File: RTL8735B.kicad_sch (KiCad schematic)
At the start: 36 parts, among them U1 W25Q128JVSIQ, U2 RTL8735BDM-A20-N04

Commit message: All key features are in the schematic.
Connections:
- net SEN_SYSCLK: now also U2.30 (SSOR_SYSCLK)
- net GPIOD_14 renamed DMIC_CLK
- net GPIOD_18 renamed DMIC_DATA
- net GPIOE_3 renamed BATT_SCL
- net GPIOE_4 renamed BATT_SDA
- net V_USB renamed +5V
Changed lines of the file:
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@@
 	(wire
 		(pts
+			(xy 123.19 135.89) (xy 123.19 163.83)
+		)
+		(stroke
+			(width 0)
+			(type default)
+		)
+	)
+	(wire
+		(pts
 			(xy 57.15 69.85) (xy 68.58 69.85)
 		)
@@
 	(wire
 		(pts
-			(xy 125.73 135.89) (xy 125.73 157.48)
+			(xy 125.73 135.89) (xy 125.73 163.83)
 		)
 		(stroke
@@
 	(wire
 		(pts
-			(xy 123.19 135.89) (xy 123.19 157.48)
-		)
-		(stroke
-			(width 0)
-			(type default)
-		)
-	)
-	(wire
-		(pts
 			(xy 143.51 21.59) (xy 143.51 24.13)
 		)
@@
 		)
 	)
-	(label "GPIOD_14"
+	(label "DMIC_CLK"
 		(at 100.33 158.75 90)
 		(effects
@@
 		)
 	)
-	(label "GPIOD_18"
+	(label "DMIC_DATA"
 		(at 110.49 158.75 90)
 		(effects
@@
 	(global_label "SEN_SYSCLK"
 		(shape input)
-		(at 127 162.56 270)
+		(at 97.79 163.83 270)
 		(fields_autoplaced yes)
 		(effects
@@
 		)
 		(property "Intersheetrefs" "${INTERSHEET_REFS}"
-			(at 127 177.2775 90)
+			(at 97.79 178.5475 90)
 			(effects
 				(font
@@
 		)
 	)
+	(global_label "BATT_SDA"
+		(shape input)
+		(at 125.73 163.83 270)
+		(fields_autoplaced yes)
+		(effects
+			(font
+				(size 1.27 1.27)
+			)
+			(justify right)
+		)
+		(property "Intersheetrefs" "${INTERSHEET_REFS}"
+			(at 125.73 175.6447 90)
+			(effects
+				(font
+					(size 1.27 1.27)
+				)
+				(justify right)
+				(hide yes)
+			)
+		)
+	)
 	(global_label "SEN_SDA"
 		(shape input)
@@
 		)
 	)
+	(global_label "BATT_SCL"
+		(shape input)
+		(at 123.19 163.83 270)
+		(fields_autoplaced yes)
+		(effects
+			(font
+				(size 1.27 1.27)
+			)
+			(justify right)
+		)
+		(property "Intersheetrefs" "${INTERSHEET_REFS}"
+			(at 123.19 175.5842 90)
+			(effects
+				(font
+					(size 1.27 1.27)
+				)
+				(justify right)
+				(hide yes)
+			)
+		)
+	)
 	(symbol
 		(lib_id "Device:R_US")
@@
 			)
 		)
-		(property "Value" "V_USB"
+		(property "Value" "+5V"
 			(at 147.32 13.97 0)
 			(effects

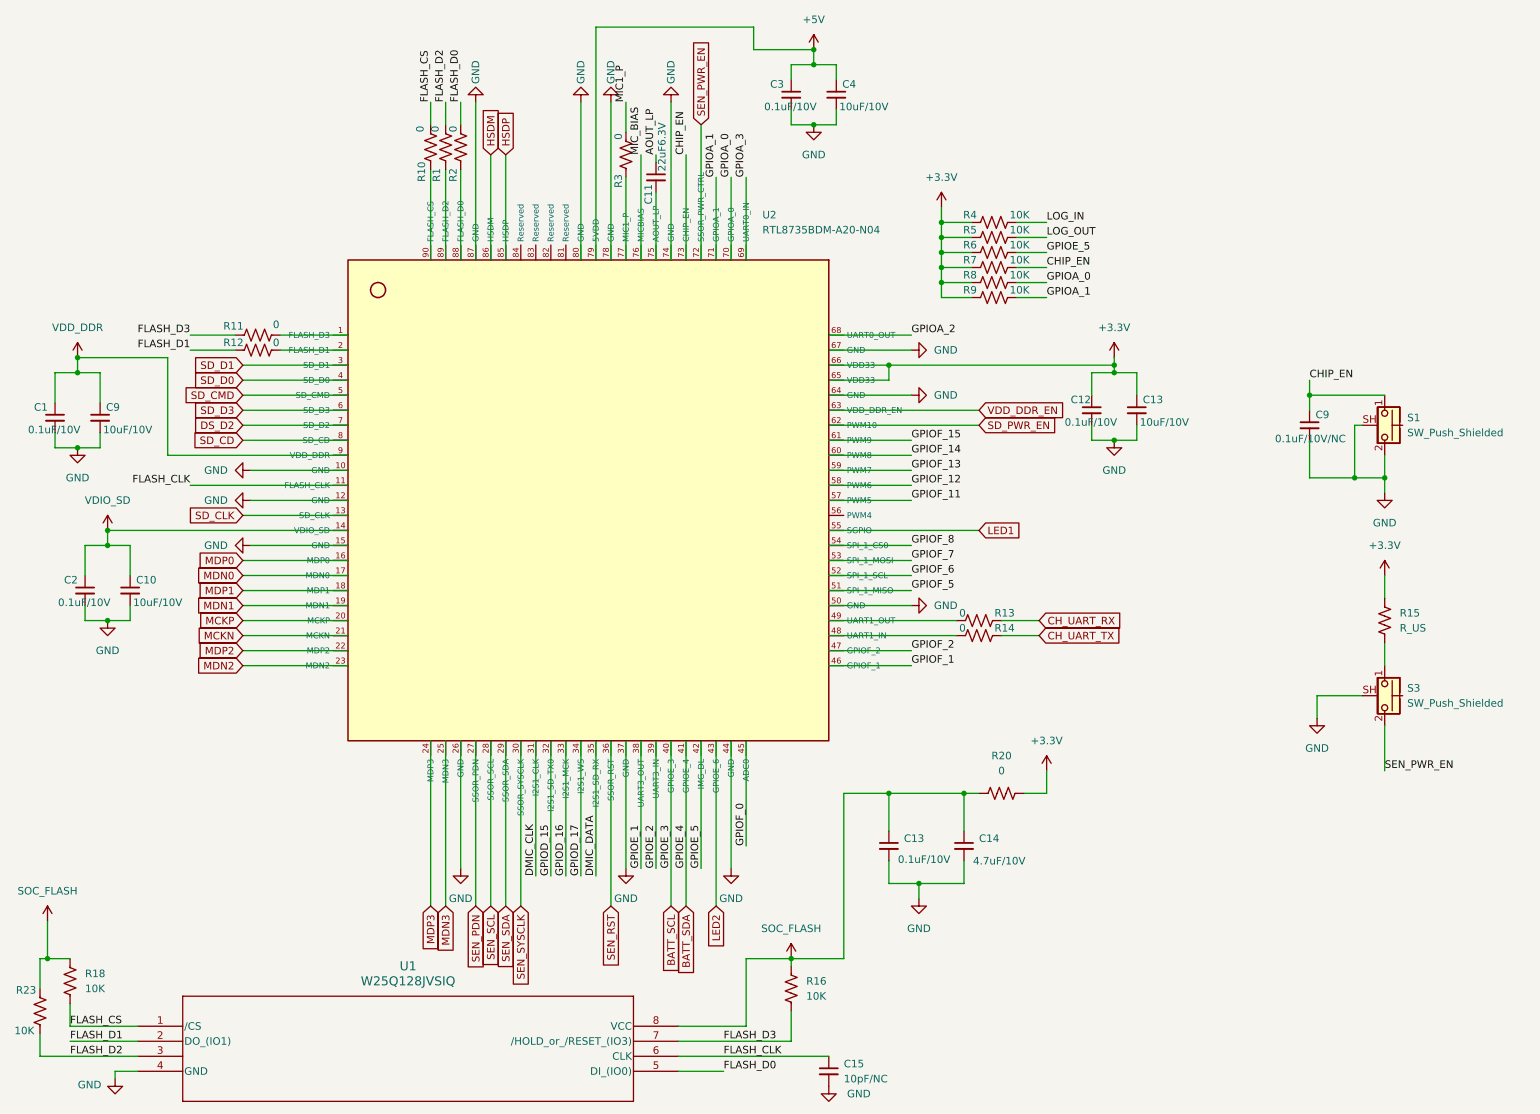
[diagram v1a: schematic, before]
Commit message: All footprints configured correctly. Next step is layout
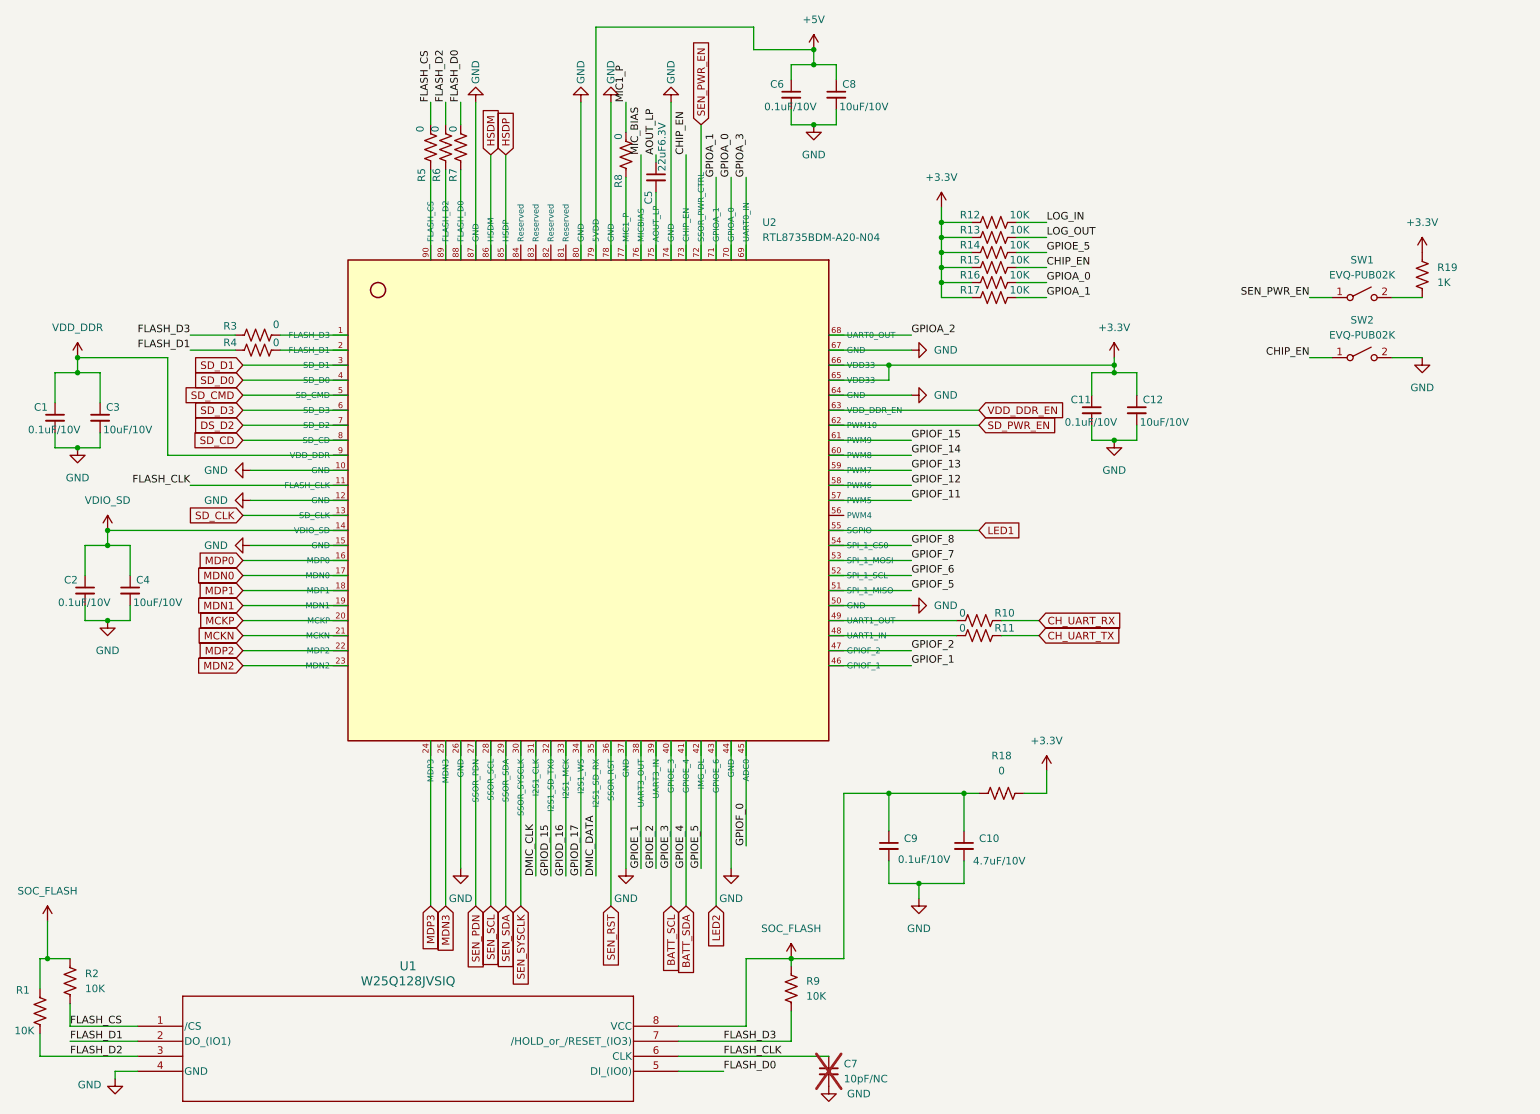
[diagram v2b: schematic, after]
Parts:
- removed C9: 0.1uF/10V/NC, symbol Device:C_Small
- removed R15: R_US, symbol Device:R_US
- removed S1, S3: SW_Push_Shielded, symbol Switch:SW_Push_Shielded
- added R19: 1K, Resistor_SMD:R_0201_0603Metric_Pad0.64x0.40mm_HandSolder, symbol Device:R_US
- added SW1, SW2: EVQ-PUB02K, Button_Switch_SMD:Panasonic_EVQPUK_EVQPUB, symbol Switch:SW_SPST
- C1, C2: footprint (none) -> Capacitor_SMD:C_0201_0603Metric_Pad0.64x0.40mm_HandSolder
- C10: renamed from C14; footprint (none) -> Capacitor_SMD:C_0201_0603Metric_Pad0.64x0.40mm_HandSolder
- C11: renamed from C12; footprint (none) -> Capacitor_SMD:C_0201_0603Metric_Pad0.64x0.40mm_HandSolder
- C12, C9: renamed from C13; footprint (none) -> Capacitor_SMD:C_0201_0603Metric_Pad0.64x0.40mm_HandSolder
- C3: renamed from C9; footprint (none) -> Capacitor_SMD:C_0201_0603Metric_Pad0.64x0.40mm_HandSolder
- C4: renamed from C10; footprint (none) -> Capacitor_SMD:C_0201_0603Metric_Pad0.64x0.40mm_HandSolder
- C5: renamed from C11; footprint (none) -> Capacitor_SMD:C_0201_0603Metric_Pad0.64x0.40mm_HandSolder
- C6: renamed from C3; footprint (none) -> Capacitor_SMD:C_0201_0603Metric_Pad0.64x0.40mm_HandSolder
- C7: renamed from C15; footprint (none) -> Capacitor_SMD:C_0201_0603Metric_Pad0.64x0.40mm_HandSolder; now not fitted
- C8: renamed from C4; footprint (none) -> Capacitor_SMD:C_0201_0603Metric_Pad0.64x0.40mm_HandSolder
- R1: renamed from R23; footprint (none) -> Resistor_SMD:R_0201_0603Metric_Pad0.64x0.40mm_HandSolder
- R10: renamed from R13; footprint (none) -> Resistor_SMD:R_0201_0603Metric_Pad0.64x0.40mm_HandSolder
- R11: renamed from R14; footprint (none) -> Resistor_SMD:R_0201_0603Metric_Pad0.64x0.40mm_HandSolder
- R12: renamed from R4; footprint (none) -> Resistor_SMD:R_0201_0603Metric_Pad0.64x0.40mm_HandSolder
- R13: renamed from R5; footprint (none) -> Resistor_SMD:R_0201_0603Metric_Pad0.64x0.40mm_HandSolder
- R14: renamed from R6; footprint (none) -> Resistor_SMD:R_0201_0603Metric_Pad0.64x0.40mm_HandSolder
- R15: renamed from R7; footprint (none) -> Resistor_SMD:R_0201_0603Metric_Pad0.64x0.40mm_HandSolder
- R16: renamed from R8; footprint (none) -> Resistor_SMD:R_0201_0603Metric_Pad0.64x0.40mm_HandSolder
- R17: renamed from R9; footprint (none) -> Resistor_SMD:R_0201_0603Metric_Pad0.64x0.40mm_HandSolder
- R18: renamed from R20; footprint (none) -> Resistor_SMD:R_0201_0603Metric_Pad0.64x0.40mm_HandSolder
- R2: renamed from R18; footprint (none) -> Resistor_SMD:R_0201_0603Metric_Pad0.64x0.40mm_HandSolder
- R3: renamed from R11; footprint (none) -> Resistor_SMD:R_0201_0603Metric_Pad0.64x0.40mm_HandSolder
- R4: renamed from R12; footprint (none) -> Resistor_SMD:R_0201_0603Metric_Pad0.64x0.40mm_HandSolder
- R5: renamed from R10; footprint (none) -> Resistor_SMD:R_0201_0603Metric_Pad0.64x0.40mm_HandSolder
- R6: renamed from R1; footprint (none) -> Resistor_SMD:R_0201_0603Metric_Pad0.64x0.40mm_HandSolder
- R7: renamed from R2; footprint (none) -> Resistor_SMD:R_0201_0603Metric_Pad0.64x0.40mm_HandSolder
- R8: renamed from R3; footprint (none) -> Resistor_SMD:R_0201_0603Metric_Pad0.64x0.40mm_HandSolder
- R9: renamed from R16; footprint (none) -> Resistor_SMD:R_0201_0603Metric_Pad0.64x0.40mm_HandSolder
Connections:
- net +3.3V: now also R19.1
- net CHIP_EN: now also SW2.1 (A)
- net GND: now also SW2.2 (B)
- net SEN_PWR_EN: now also SW1.1 (A)
- new net: R19.2, SW1.2 (B)

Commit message: In the middle of layout. WIP
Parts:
- C1, C11, C2, C6, C9: value 0.1uF/10V -> 0.1uF
- C10: value 4.7uF/10V -> 4.7uF
- C12, C3, C4, C8: value 10uF/10V -> 10uF
- C5: value 22uF6.3V -> 22uF
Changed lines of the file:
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@@
 			)
 		)
-		(property "Value" "4.7uF/10V"
+		(property "Value" "4.7uF"
 			(at 174.244 156.21 0)
 			(effects
@@
 			)
 		)
-		(property "Value" "0.1uF/10V"
+		(property "Value" "0.1uF"
 			(at 19.558 112.522 0)
 			(effects
@@
 			)
 		)
-		(property "Value" "10uF/10V"
+		(property "Value" "10uF"
 			(at 32.258 112.522 0)
 			(effects
@@
 			)
 		)
-		(property "Value" "0.1uF/10V"
+		(property "Value" "0.1uF"
 			(at 189.738 82.042 0)
 			(effects
@@
 			)
 		)
-		(property "Value" "0.1uF/10V"
+		(property "Value" "0.1uF"
 			(at 161.544 155.956 0)
 			(effects
@@
 			)
 		)
-		(property "Value" "10uF/10V"
+		(property "Value" "10uF"
 			(at 202.438 82.042 0)
 			(effects
@@
 			)
 		)
-		(property "Value" "10uF/10V"
+		(property "Value" "10uF"
 			(at 151.638 28.702 0)
 			(effects
@@
 			)
 		)
-		(property "Value" "22uF6.3V"
+		(property "Value" "22uF"
 			(at 121.666 39.624 90)
 			(effects
@@
 			)
 		)
-		(property "Value" "0.1uF/10V"
+		(property "Value" "0.1uF"
 			(at 138.938 28.702 0)
 			(effects
@@
 			)
 		)
-		(property "Value" "0.1uF/10V"
+		(property "Value" "0.1uF"
 			(at 14.478 83.312 0)
 			(effects
@@
 			)
 		)
-		(property "Value" "10uF/10V"
+		(property "Value" "10uF"
 			(at 27.178 83.312 0)
 			(effects

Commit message: Breakthrough in PCB layout. WIP
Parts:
- removed R10, R11, R18, R3, R4, R5, R6, R7, R8: 0, Resistor_SMD:R_0201_0603Metric_Pad0.64x0.40mm_HandSolder, symbol Device:R_US
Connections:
- net LOG_IN is gone; now on net CH_UART_TX: R12.2
- net LOG_OUT is gone; now on net CH_UART_RX: R13.2
- net SOC_FLASH is gone; now on net +3.3V: C10.1, C9.1, R1.1, R2.1, R9.1, U1.8 (VCC)
- net CH_UART_RX: now also U2.49 (UART1_OUT)
- net CH_UART_TX: now also U2.48 (UART1_IN)
- net FLASH_CS: now also U2.90 (FLASH_CS)
- net FLASH_D0: now also U2.88 (FLASH_D0)
- net FLASH_D1: now also U2.2 (FLASH_D1)
- net FLASH_D2: now also U2.89 (FLASH_D2)
- net FLASH_D3: now also U2.1 (FLASH_D3)
- net MIC1_P: now also U2.77 (MIC1_P)
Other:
- moved on the sheet: C10, R9

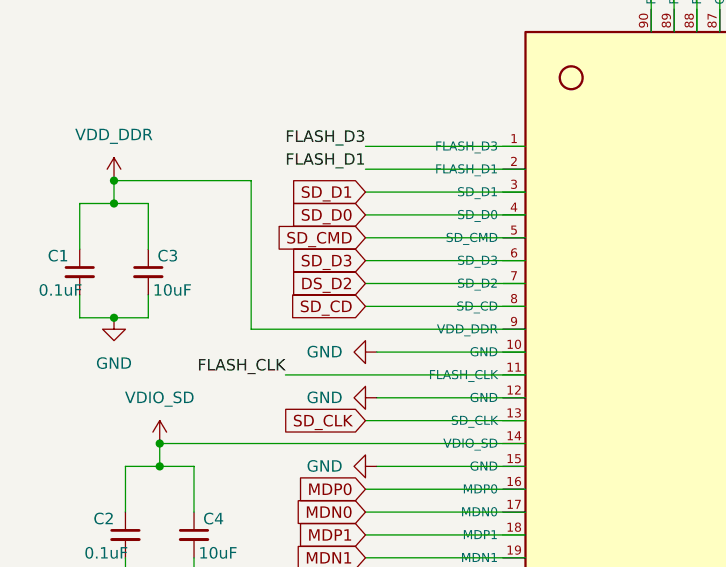
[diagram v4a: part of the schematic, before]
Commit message: Most signals routed. Just need power plane clean up and final checks. Almost there, but WIP
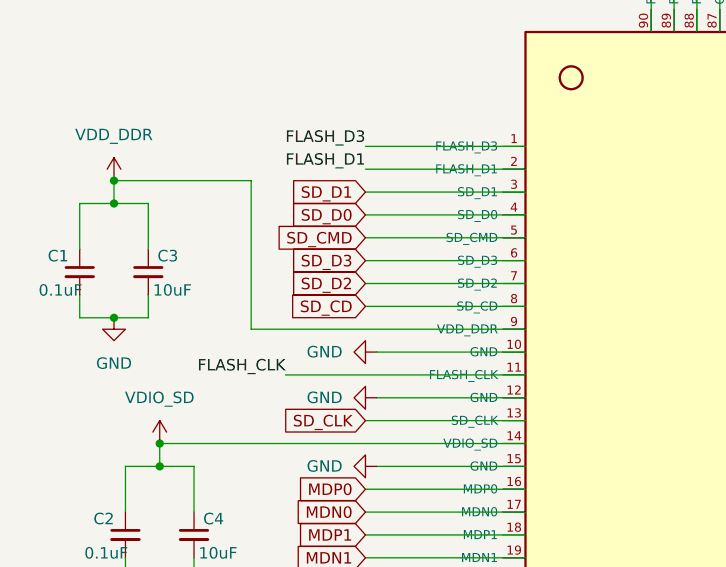
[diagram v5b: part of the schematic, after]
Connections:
- net DS_D2 renamed SD_D2
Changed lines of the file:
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@@
 		)
 	)
-	(global_label "DS_D2"
+	(global_label "SD_D2"
 		(shape input)
 		(at 50.8 82.55 180)
